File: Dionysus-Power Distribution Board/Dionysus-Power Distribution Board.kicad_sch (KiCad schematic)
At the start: 0 parts

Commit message: Added Libraries and Copied previous work
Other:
- sheet Power Management Controller: file Power Management Controller.kicad_sch.kicad_sch -> Power Management Controller.kicad_sch
- title: Power Distribution Board, Dionysus -> (none)
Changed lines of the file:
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@@
 (kicad_sch (version 20230121) (generator eeschema)
   (paper "B")
-  (title_block
-    (title "Power Distribution Board, Dionysus")
-    (rev "alpha")
-    (comment 1 "J. LENDI")
-    (comment 2 "PROTOTYPE - ALPHA")
-  )
-  (sheet (at 38.1 25.4) (size 38.1 12.7) (fields_autoplaced)
-    (stroke (width 0.1524) (type solid))
-    (fill (color 0 0 0 0.0000))
-    (property "Sheetname" "Power Management Controller" (at 38.1 24.6884 0)
-      (effects (font (size 1.27 1.27)) (justify left bottom))
+  (sheet (at 101.6 25.4) (size 25.4 25.4)
+    (stroke (width 0.254) (type solid))
+    (fill (color 255 255 194 1.0000))
+    (property "Sheetname" "Pulse Width Modulation Controller" (at 101.6 24.6376 0)
+      (effects (font (size 1.27 1.27) bold) (justify left bottom))
     )
-    (property "Sheetfile" "Power Management Controller.kicad_sch.kicad_sch" (at 38.1 38.6846 0)
+    (property "Sheetfile" "Pulse Width Modulation Controller.kicad_sch" (at 101.6 51.4354 0)
       (effects (font (size 1.27 1.27)) (justify left top) hide)
     )
     (instances
       (project "Dionysus-Power Distribution Board"
-        (path "/abe21820-8071-4530-921a-b389cdc1b29d" (page "2"))
+        (path "/348c5b44-eb44-4a1f-9b5c-5ed28bc510c5" (page "3"))
       )
     )
   )
-  (sheet (at 38.1 50.8) (size 38.1 12.7) (fields_autoplaced)
-    (stroke (width 0.1524) (type solid))
-    (fill (color 0 0 0 0.0000))
-    (property "Sheetname" "Pulse Width Modulation Controller" (at 38.1 50.0884 0)
-      (effects (font (size 1.27 1.27)) (justify left bottom))
+  (sheet (at 152.4 25.4) (size 25.4 25.4) (fields_autoplaced)
+    (stroke (width 0.254) (type solid))
+    (fill (color 255 255 194 1.0000))
+    (property "Sheetname" "GPIO" (at 152.4 24.6376 0)
+      (effects (font (size 1.27 1.27) bold) (justify left bottom))
     )
-    (property "Sheetfile" "Pulse Width Modulation Controller.kicad_sch" (at 38.1 64.0846 0)
+    (property "Sheetfile" "GPIO.kicad_sch" (at 152.4 51.4354 0)
       (effects (font (size 1.27 1.27)) (justify left top) hide)
     )
     (instances
       (project "Dionysus-Power Distribution Board"
-        (path "/abe21820-8071-4530-921a-b389cdc1b29d" (page "3"))
+        (path "/348c5b44-eb44-4a1f-9b5c-5ed28bc510c5" (page "5"))
       )
     )
   )
-  (sheet (at 38.1 76.2) (size 38.1 12.7) (fields_autoplaced)
-    (stroke (width 0.1524) (type solid))
-    (fill (color 0 0 0 0.0000))
-    (property "Sheetname" "GPIO" (at 38.1 75.4884 0)
-      (effects (font (size 1.27 1.27)) (justify left bottom))
+  (sheet (at 203.2 25.4) (size 25.4 25.4) (fields_autoplaced)
+    (stroke (width 0.254) (type solid))
+    (fill (color 255 255 194 1.0000))
+    (property "Sheetname" "System Sensor" (at 203.2 24.6376 0)
+      (effects (font (size 1.27 1.27) bold) (justify left bottom))
     )
-    (property "Sheetfile" "GPIO.kicad_sch" (at 38.1 89.4846 0)
+    (property "Sheetfile" "System Sensor.kicad_sch" (at 203.2 51.4354 0)
       (effects (font (size 1.27 1.27)) (justify left top) hide)
     )
     (instances
       (project "Dionysus-Power Distribution Board"
-        (path "/abe21820-8071-4530-921a-b389cdc1b29d" (page "5"))
+        (path "/348c5b44-eb44-4a1f-9b5c-5ed28bc510c5" (page "4"))
       )
     )
   )
-  (sheet (at 38.1 101.6) (size 38.1 12.7) (fields_autoplaced)
-    (stroke (width 0.1524) (type solid))
-    (fill (color 0 0 0 0.0000))
-    (property "Sheetname" "System Sensor" (at 38.1 100.8884 0)
-      (effects (font (size 1.27 1.27)) (justify left bottom))
+  (sheet (at 50.8 25.4) (size 25.4 25.4) (fields_autoplaced)
+    (stroke (width 0.254) (type solid))
+    (fill (color 255 255 194 1.0000))
+    (property "Sheetname" "Power Management Controller" (at 50.8 24.6376 0)
+      (effects (font (size 1.27 1.27) bold) (justify left bottom))
     )
-    (property "Sheetfile" "System Sensor.kicad_sch" (at 38.1 114.8846 0)
+    (property "Sheetfile" "Power Management Controller.kicad_sch" (at 50.8 51.4354 0)
       (effects (font (size 1.27 1.27)) (justify left top) hide)
     )
     (instances
       (project "Dionysus-Power Distribution Board"
-        (path "/abe21820-8071-4530-921a-b389cdc1b29d" (page "4"))
+        (path "/348c5b44-eb44-4a1f-9b5c-5ed28bc510c5" (page "2"))
       )
     )

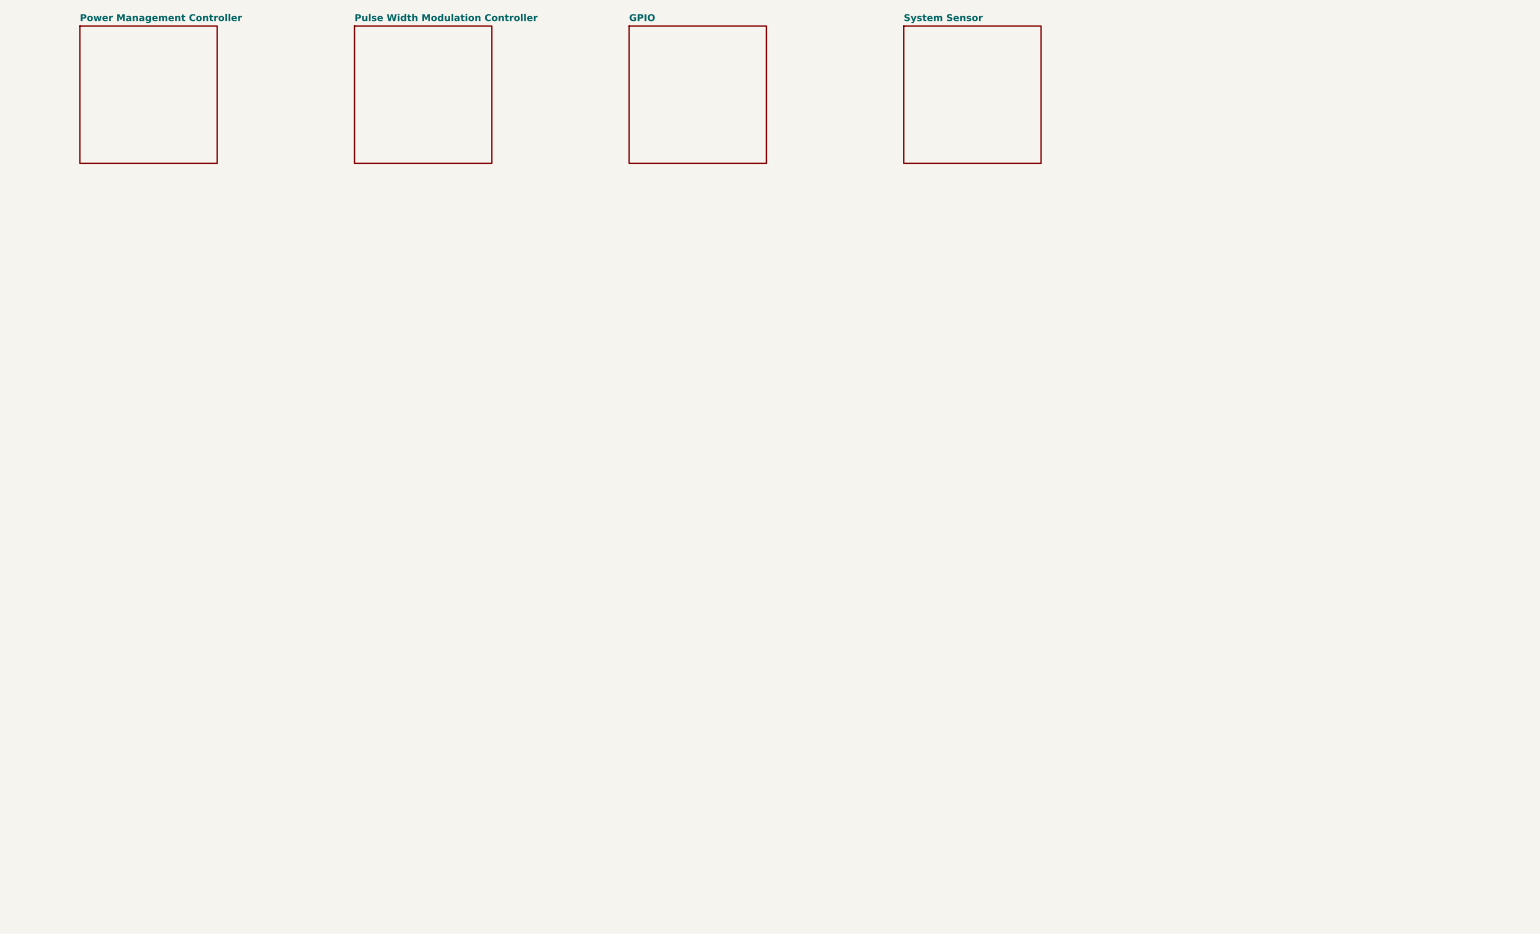
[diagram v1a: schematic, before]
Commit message: Updated Symbols and Redefined Hierarchical Pins
Updated high side driver symbols, and added hierarchical pins to page 1
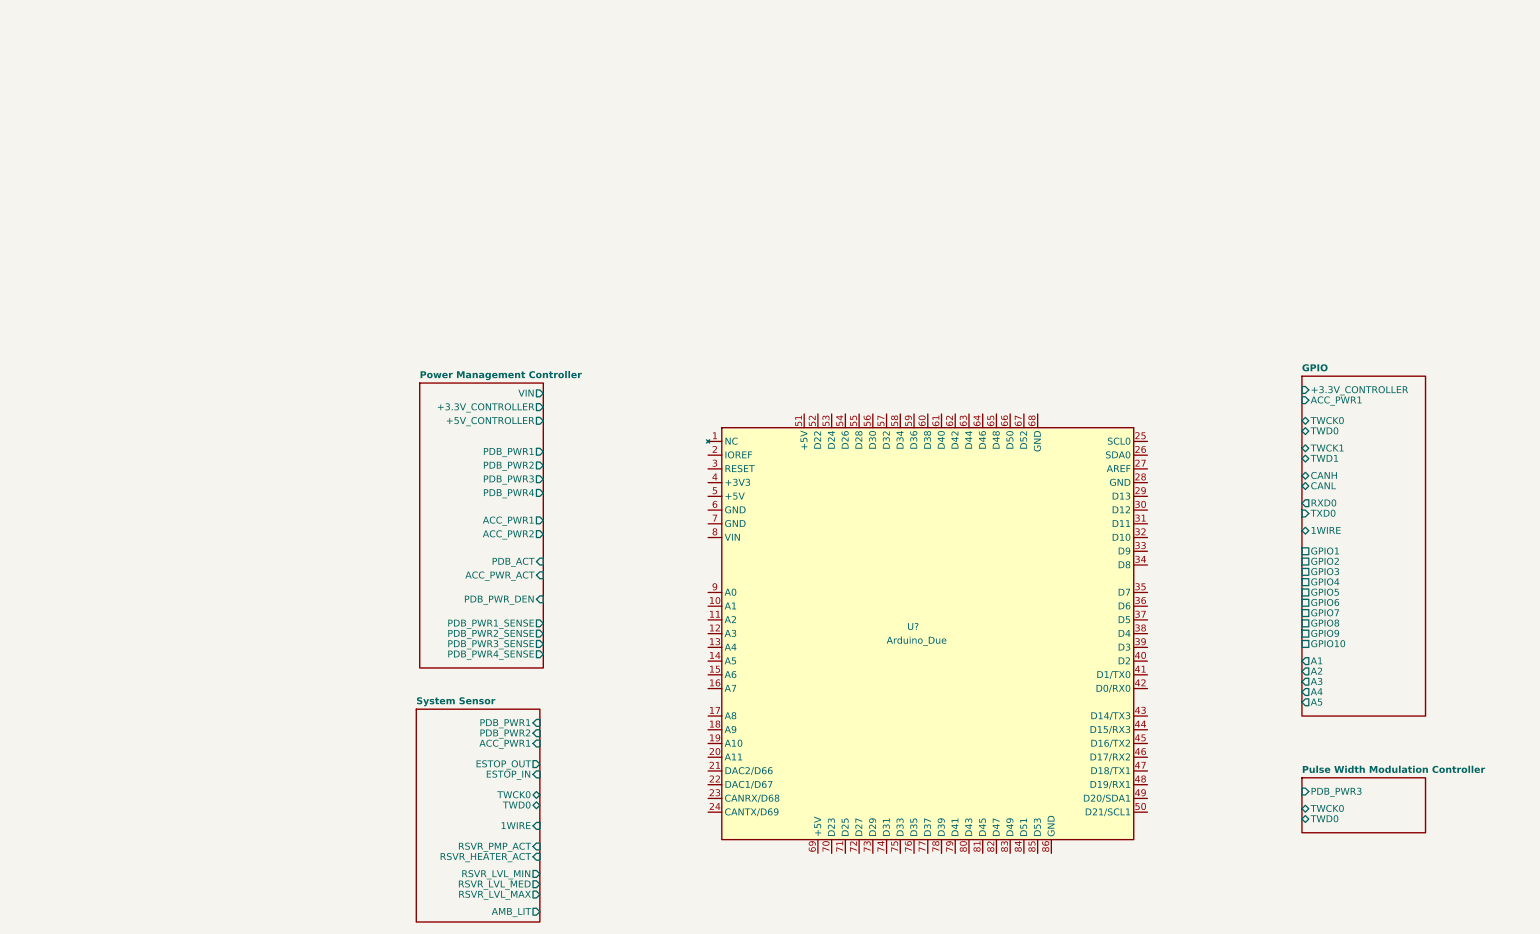
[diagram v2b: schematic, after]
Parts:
- added U?: Arduino_Due, symbol MCU_Module_jal:Arduino_Due
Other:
- sheet GPIO ports: added +3.3V_CONTROLLER, 1WIRE, A1, A2, A3, A4, A5, ACC_PWR1, CANH, CANL, GPIO1, GPIO10, GPIO2, GPIO3, GPIO4, GPIO5, GPIO6, GPIO7, GPIO8, GPIO9, RXD0, TWCK0, TWCK1, TWD0, TWD1, TXD0; removed none
- sheet Power Management Controller ports: added +3.3V_CONTROLLER, +5V_CONTROLLER, ACC_PWR1, ACC_PWR2, ACC_PWR_ACT, PDB_ACT, PDB_PWR1, PDB_PWR1_SENSE, PDB_PWR2, PDB_PWR2_SENSE, PDB_PWR3, PDB_PWR3_SENSE, PDB_PWR4, PDB_PWR4_SENSE, PDB_PWR_DEN, VIN; removed none
- sheet Pulse Width Modulation Controller ports: added PDB_PWR3, TWCK0, TWD0; removed none
- sheet System Sensor ports: added 1WIRE, ACC_PWR1, AMB_LIT, ESTOP_IN, ESTOP_OUT, PDB_PWR1, PDB_PWR2, RSVR_HEATER_ACT, RSVR_LVL_MAX, RSVR_LVL_MED, RSVR_LVL_MIN, RSVR_PMP_ACT, TWCK0, TWD0; removed none
